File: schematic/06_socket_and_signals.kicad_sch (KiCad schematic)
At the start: 16 parts, among them J1 280-5205-01, J2 Original 6-pin JTAG, J5 MASTER CLOCK SMA, J6 20-pin JTAG: same pinout, J601 Differential probe: high Z, Q601 MMBT3904, SW601 DUT RESET

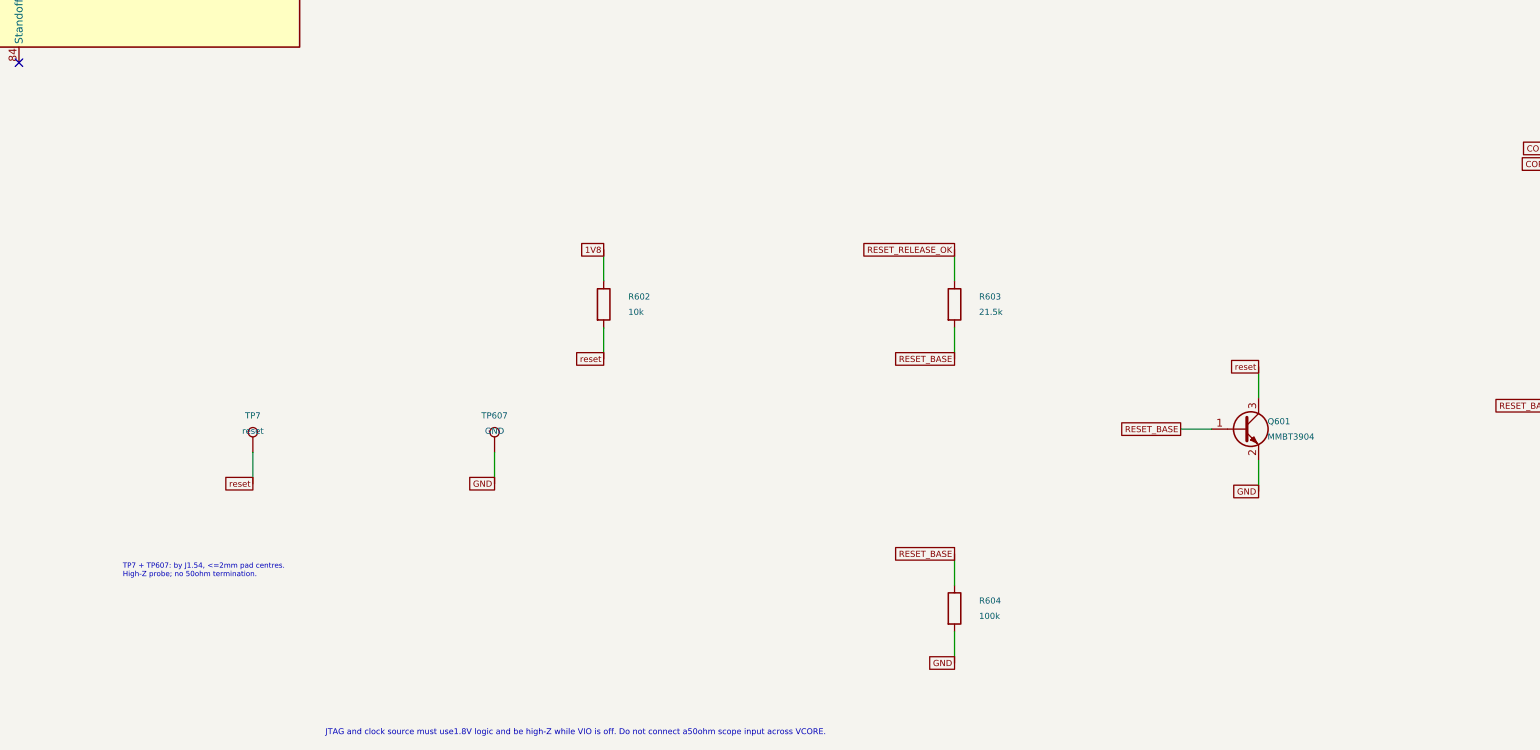
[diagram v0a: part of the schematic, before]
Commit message: Decouple DUT reset and input diagnostics from power interlocks
Use explicit manual, ZedBoard, and Pico reset requests. Route input-voltage validity to telemetry while retaining protective power interlocks. Synchronize requirements, schematic exports, BOM, and verification evidence.
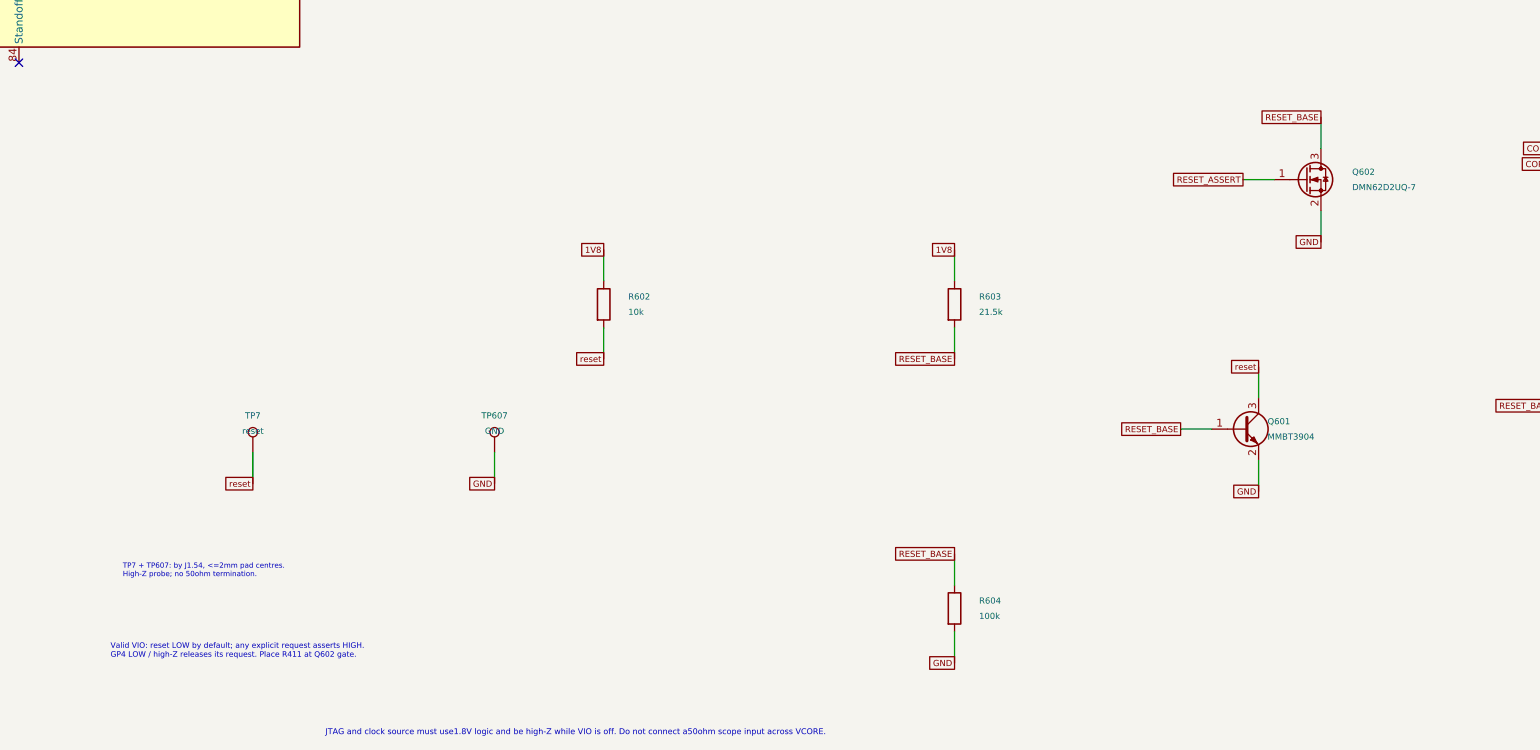
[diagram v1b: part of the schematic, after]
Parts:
- added Q602: DMN62D2UQ-7, Sphinx_V2:Package_TO_SOT_SMD__SOT-23, symbol Sphinx_V2:Transistor_FET__Q_NMOS_GSD
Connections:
- net RESET_RELEASE_OK is gone; now on net 1V8: R603.1
- net GND: now also Q602.2 (S)
- net RESET_BASE: now also Q602.3 (D)
- new net RESET_ASSERT: Q602.1 (G)
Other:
- note added: "Valid VIO: reset LOW by default; any explicit request asserts HIGH. GP4 LOW / high-Z releases its request. Place R411 at Q602 gate."
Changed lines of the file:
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@@
 (kicad_sch (version 20250114) (generator "eeschema") (generator_version "10.0")
  (paper "A3")
-        (title_block (title "06 | Socket pinout and signal interfaces") (date "2026-09-19") (rev "V2")
+        (title_block (title "06 | Socket pinout and signal interfaces") (date "2026-09-20") (rev "V2")
         (company "Sphinx | Programmable power test board")
         (comment 1 "Review package: PCB, PI, SI, thermal and ASIC limits require qualification")
@@
 (property "Datasheet" "https://yageogroup.com/component-documentation/download/specsheet/RC0603FR-0710KL" (at 180.34 205.74 0) (effects (font (size 1.0 1.0))  (hide yes)))
 (property "MPN" "RC0603FR-0710KL" (at 180.34 205.74 0) (effects (font (size 1.0 1.0))  (hide yes)))
-(property "Description" "Active-high reset: pull high while control not ready | 10k +/-1% 0.1W 0603 thick film; +/-100ppm/C" (at 180.34 205.74 0) (effects (font (size 1.0 1.0))  (hide yes)))
+(property "Description" "Pulls active-high DUT reset up when Q601 is inhibited by an explicit reset request | 10k +/-1% 0.1W 0603 thick film; +/-100ppm/C" (at 180.34 205.74 0) (effects (font (size 1.0 1.0))  (hide yes)))
 (pin "1")
 (pin "2")
@@
 (property "Datasheet" "https://yageogroup.com/component-documentation/download/specsheet/RC0603FR-0721K5L" (at 237.49 205.74 0) (effects (font (size 1.0 1.0))  (hide yes)))
 (property "MPN" "RC0603FR-0721K5L" (at 237.49 205.74 0) (effects (font (size 1.0 1.0))  (hide yes)))
-(property "Description" "Limits optocoupler sink demand below0.2mA; retains Q601 base drive for the0.18mA reset pull-up | 21.5k +/-1% 0.1W 0603 thick film; +/-100ppm/C" (at 237.49 205.74 0) (effects (font (size 1.0 1.0))  (hide yes)))
+(property "Description" "VIO bias defaults Q601 on and reset released; explicit reset sink current about84uA at1.8V | 21.5k +/-1% 0.1W 0603 thick film; +/-100ppm/C" (at 237.49 205.74 0) (effects (font (size 1.0 1.0))  (hide yes)))
 (pin "1")
 (pin "2")
 (instances (project "sphinx_power_v2" (path "/f39c8d6a-e478-5a84-9c95-766dfa82ae02/d57f165e-6d05-5f9f-9c4a-9dc401e097b2" (reference "R603") (unit 1)))) )
 (wire (pts (xy 237.49 201.93) (xy 237.49 196.85)) (stroke (width 0) (type default)))
-(global_label "RESET_RELEASE_OK" (shape passive) (at 237.49 196.85 180) (effects (font (size 1.0 1.0)) (justify right) ) (property "Intersheetrefs" "${INTERSHEET_REFS}" (at 237.49 196.85 180) (effects (font (size 0.8 0.8))  (hide yes))))
+(global_label "1V8" (shape passive) (at 237.49 196.85 180) (effects (font (size 1.0 1.0)) (justify right) ) (property "Intersheetrefs" "${INTERSHEET_REFS}" (at 237.49 196.85 180) (effects (font (size 0.8 0.8))  (hide yes))))
 (wire (pts (xy 237.49 209.55) (xy 237.49 214.63)) (stroke (width 0) (type default)))
 (global_label "RESET_BASE" (shape passive) (at 237.49 214.63 180) (effects (font (size 1.0 1.0)) (justify right) ) (property "Intersheetrefs" "${INTERSHEET_REFS}" (at 237.49 214.63 180) (effects (font (size 0.8 0.8))  (hide yes))))
@@
 (property "Datasheet" "https://www.diodes.com/assets/Datasheets/MMBT3904.pdf" (at 284.48 226.06 0) (effects (font (size 1.0 1.0))  (hide yes)))
 (property "MPN" "MMBT3904-7-F" (at 284.48 226.06 0) (effects (font (size 1.0 1.0))  (hide yes)))
-(property "Description" "Open collector reset release. No3.3V connection to DUT reset pin. | NPN SOT23; pin1=B, pin2=E, pin3=C" (at 284.48 226.06 0) (effects (font (size 1.0 1.0))  (hide yes)))
+(property "Description" "VIO-biased default reset release; SW601, U601 or Q602 sink its base to assert reset. No3.3V connection to DUT reset pin. | NPN SOT23; pin1=B, pin2=E, pin3=C" (at 284.48 226.06 0) (effects (font (size 1.0 1.0))  (hide yes)))
 (pin "1")
 (pin "2")
@@
 (global_label "GND" (shape passive) (at 162.56 234.95 180) (effects (font (size 1.0 1.0)) (justify right) ) (property "Intersheetrefs" "${INTERSHEET_REFS}" (at 162.56 234.95 180) (effects (font (size 0.8 0.8))  (hide yes))))
 (text "TP7 + TP607: by J1.54, <=2mm pad centres.\nHigh-Z probe; no 50ohm termination." (at 102 248 0) (effects (font (size 0.85 0.85)) (justify left top) ))
-(text "JTAG and clock source must use1.8V logic and be high-Z while VIO is off. Do not connect a50ohm scope input across VCORE." (at 135 275 0) (effects (font (size 0.95 0.95)) (justify left top) ))(sheet_instances (path "/f39c8d6a-e478-5a84-9c95-766dfa82ae02/d57f165e-6d05-5f9f-9c4a-9dc401e097b2" (page "7"))) (embedded_fonts no))
+(text "JTAG and clock source must use1.8V logic and be high-Z while VIO is off. Do not connect a50ohm scope input across VCORE." (at 135 275 0) (effects (font (size 0.95 0.95)) (justify left top) ))(sheet_instances (path "/f39c8d6a-e478-5a84-9c95-766dfa82ae02/d57f165e-6d05-5f9f-9c4a-9dc401e097b2" (page "7"))) (embedded_fonts no)
+(symbol (lib_id "Sphinx_V2:Transistor_FET__Q_NMOS_GSD") (at 294.64 185.42 0) (unit 1) (exclude_from_sim no) (in_bom yes) (on_board yes) (dnp no)
+(property "Reference" "Q602" (at 302.26 184.17 0) (effects (font (size 1.0 1.0)) (justify left) ))
+(property "Value" "DMN62D2UQ-7" (at 302.26 186.67 0) (effects (font (size 1.0 1.0)) (justify left) ))
+(property "Footprint" "Sphinx_V2:Package_TO_SOT_SMD__SOT-23" (at 294.64 185.42 0) (effects (font (size 1.0 1.0))  (hide yes)))
+(property "Datasheet" "https://www.diodes.com/assets/Datasheets/DMN62D2UQ.pdf" (at 294.64 185.42 0) (effects (font (size 1.0 1.0))  (hide yes)))
+(property "MPN" "DMN62D2UQ-7" (at 294.64 185.42 0) (effects (font (size 1.0 1.0))  (hide yes)))
+(property "Description" "Pico active-high reset request sinks RESET_BASE; R411100k gate pulldown must be placed next to Q602. | 60V NMOS, +/-20V VGS, SOT23 G1/S2/D3; RDS(on)<=4Ohm atVGS1.8V/25C; -55..150C operating range; full-temperature electrical maxima not generally specified" (at 294.64 185.42 0) (effects (font (size 1.0 1.0))  (hide yes)))
+(pin "1")
+(pin "2")
+(pin "3")
+(instances (project "sphinx_power_v2" (path "/f39c8d6a-e478-5a84-9c95-766dfa82ae02/d57f165e-6d05-5f9f-9c4a-9dc401e097b2" (reference "Q602") (unit 1)))) )
+(wire (pts (xy 289.56 185.42) (xy 284.48 185.42)) (stroke (width 0) (type default)))
+(global_label "RESET_ASSERT" (shape passive) (at 284.48 185.42 180) (effects (font (size 1.0 1.0)) (justify right)) (property "Intersheetrefs" "${INTERSHEET_REFS}" (at 284.48 185.42 180) (effects (font (size 0.8 0.8)) (hide yes))))
+(wire (pts (xy 297.18 180.34) (xy 297.18 175.26)) (stroke (width 0) (type default)))
+(global_label "RESET_BASE" (shape passive) (at 297.18 175.26 180) (effects (font (size 1.0 1.0)) (justify right)) (property "Intersheetrefs" "${INTERSHEET_REFS}" (at 297.18 175.26 180) (effects (font (size 0.8 0.8)) (hide yes))))
+(wire (pts (xy 297.18 190.50) (xy 297.18 195.58)) (stroke (width 0) (type default)))
+(global_label "GND" (shape passive) (at 297.18 195.58 180) (effects (font (size 1.0 1.0)) (justify right)) (property "Intersheetrefs" "${INTERSHEET_REFS}" (at 297.18 195.58 180) (effects (font (size 0.8 0.8)) (hide yes))))
+(text "Valid VIO: reset LOW by default; any explicit request asserts HIGH.\nGP4 LOW / high-Z releases its request. Place R411 at Q602 gate." (at 100 261 0) (effects (font (size 0.9 0.9)) (justify left top)))
+)

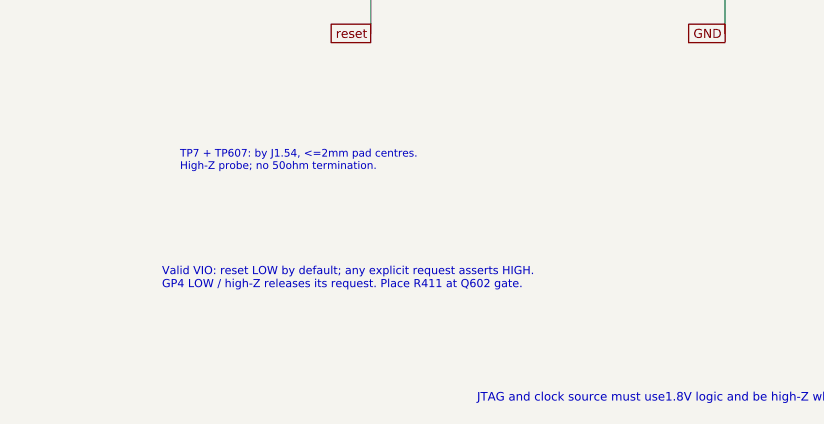
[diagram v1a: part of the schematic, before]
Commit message: Make V2 power state independent of Pico
Add an independently powered retained control domain, isolated I2C, hardware temperature and I/O overvoltage protection, and correct the socket keepout. Align operating requirements, BOM, schematic exports, and validation evidence.

Complete the final source review: zero ERC violations, 247 footprint/BOM matches, 80 ASIC pin checks, and 51 companion host tests including 122 interrupted-write cases. Record physical qualification limits and external companion firmware hashes.
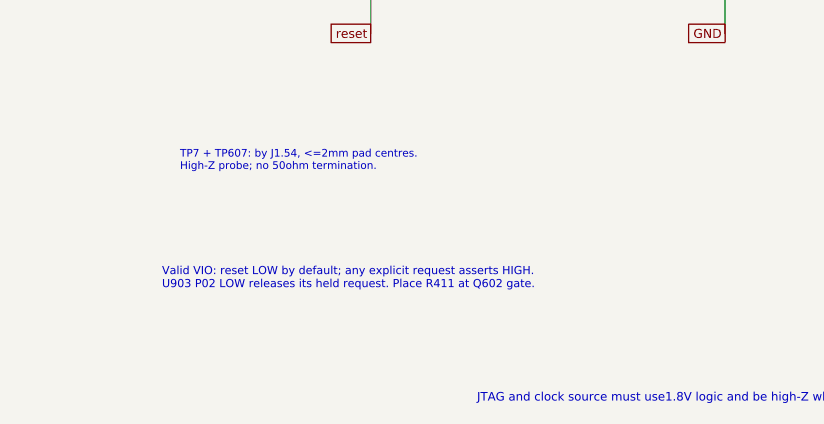
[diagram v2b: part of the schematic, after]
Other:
- note added: "Valid VIO: reset LOW by default; any explicit request asserts HIGH. U903 P02 LOW releases its held request. Place R411 at Q602 gate."
- note removed: "Valid VIO: reset LOW by default; any explicit request asserts HIGH. GP4 LOW / high-Z releases its request. Place R411 at Q602 gate."
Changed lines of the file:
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@@
 (kicad_sch (version 20250114) (generator "eeschema") (generator_version "10.0")
  (paper "A3")
-        (title_block (title "06 | Socket pinout and signal interfaces") (date "2026-09-20") (rev "V2")
+        (title_block (title "06 | Socket pinout and signal interfaces") (date "2026-09-22") (rev "V2")
         (company "Sphinx | Programmable power test board")
         (comment 1 "Review package: PCB, PI, SI, thermal and ASIC limits require qualification")
@@
 (property "Datasheet" "https://www.diodes.com/assets/Datasheets/DMN62D2UQ.pdf" (at 294.64 185.42 0) (effects (font (size 1.0 1.0))  (hide yes)))
 (property "MPN" "DMN62D2UQ-7" (at 294.64 185.42 0) (effects (font (size 1.0 1.0))  (hide yes)))
-(property "Description" "Pico active-high reset request sinks RESET_BASE; R411100k gate pulldown must be placed next to Q602. | 60V NMOS, +/-20V VGS, SOT23 G1/S2/D3; RDS(on)<=4Ohm atVGS1.8V/25C; -55..150C operating range; full-temperature electrical maxima not generally specified" (at 294.64 185.42 0) (effects (font (size 1.0 1.0))  (hide yes)))
+(property "Description" "Held U903 active-high reset request sinks RESET_BASE; R411100k gate pulldown must be placed next to Q602. | 60V NMOS, +/-20V VGS, SOT23 G1/S2/D3; RDS(on)<=4Ohm atVGS1.8V/25C; -55..150C operating range; full-temperature electrical maxima not generally specified" (at 294.64 185.42 0) (effects (font (size 1.0 1.0))  (hide yes)))
 (pin "1")
 (pin "2")
@@
 (wire (pts (xy 297.18 190.50) (xy 297.18 195.58)) (stroke (width 0) (type default)))
 (global_label "GND" (shape passive) (at 297.18 195.58 180) (effects (font (size 1.0 1.0)) (justify right)) (property "Intersheetrefs" "${INTERSHEET_REFS}" (at 297.18 195.58 180) (effects (font (size 0.8 0.8)) (hide yes))))
-(text "Valid VIO: reset LOW by default; any explicit request asserts HIGH.\nGP4 LOW / high-Z releases its request. Place R411 at Q602 gate." (at 100 261 0) (effects (font (size 0.9 0.9)) (justify left top)))
+(text "Valid VIO: reset LOW by default; any explicit request asserts HIGH.\nU903 P02 LOW releases its held request. Place R411 at Q602 gate." (at 100 261 0) (effects (font (size 0.9 0.9)) (justify left top)))
 )
